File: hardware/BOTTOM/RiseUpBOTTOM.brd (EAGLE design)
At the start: 33 x 33 mm, 31 parts, among them U1 AD5242-SO16

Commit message: Updated Bottom board from Take 2
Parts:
- added J1: (no value), LinnesLab-Connectors:1X07
- moved R17 5.33 mm to (14.0, 30.5)
- moved R22 4.16 mm to (6.15, 24.3)
- moved R16 3.93 mm to (17.7, 11.4)
- moved IMU1 3.46 mm to (13.1, 7.62)
- moved C22 3.11 mm to (21.4, 7.29)
- moved U$4 3.00 mm to (21.6, 11.0)
- moved R24 2.80 mm to (14.2, 21.0)
- moved C20 2.20 mm to (14.2, 27.2)
- moved R15 2.04 mm to (31.6, 18.3)
- moved C1 1.83 mm to (6.78, 6.53)
- moved R19 1.82 mm to (6.12, 30.5)
- moved C18 1.57 mm to (14.5, 14.4)
- moved U1 1.42 mm to (29.2, 9.45)
- moved C17 1.22 mm to (14.2, 23.6)
- moved C16 1.16 mm to (27.8, 18.3)
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
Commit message: Updates end of July2nd, Start Take 03
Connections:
- removed net LED.CTRL: U$4.8
- removed net PPG: C21.2, OP3.1, U1.14
- removed net TIA: C10.2, C15.1, OP4.1, U1.3
- new net A6/TIA: C10.2, C15.1, J1.5, OP4.1, U1.3
- new net A7/PPG: C21.2, J1.7, OP3.1, U1.14
- new net D29/LED.CTRL: J1.6, U$4.8
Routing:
- added copper zone on layer 16, net GDN
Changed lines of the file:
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@@
 <setting verticaltext="up"/>
 </settings>
-<grid distance="1" unitdist="mil" unit="mm" style="lines" multiple="1" display="no" altdistance="5" altunitdist="mil" altunit="mil"/>
+<grid distance="0.1" unitdist="mil" unit="mil" style="lines" multiple="1" display="no" altdistance="5" altunitdist="mil" altunit="mil"/>
 <layers>
 <layer number="1" name="Top" color="4" fill="1" visible="yes" active="yes"/>
@@
 <wire x1="9.7028" y1="20.2332" x2="10.6528" y2="20.2332" width="0" layer="19" extent="1-1"/>
 <wire x1="13.6026" y1="14.3764" x2="10.6528" y2="20.2332" width="0" layer="19" extent="1-1"/>
-<wire x1="5.2968" y1="26.5684" x2="13.3994" y2="23.6474" width="0" layer="19" extent="1-1"/>
-<wire x1="5.2714" y1="30.48" x2="5.2968" y2="26.5684" width="0" layer="19" extent="1-1"/>
 <wire x1="10.5156" y1="8.89" x2="13.6026" y2="14.3764" width="0" layer="19" extent="1-1"/>
 <wire x1="6.7818" y1="7.3778" x2="10.5156" y2="8.89" width="0" layer="19" extent="1-1"/>
-<wire x1="21.9502" y1="9.7964" x2="13.6026" y2="14.3764" width="0" layer="19" extent="1-1"/>
+<wire x1="5.2968" y1="26.5684" x2="9.7028" y2="20.2332" width="0" layer="19" extent="1-1"/>
+<wire x1="5.2714" y1="30.48" x2="5.2968" y2="26.5684" width="0" layer="19" extent="1-1"/>
+<wire x1="22.794" y1="15.4592" x2="20.27" y2="24.08" width="0" layer="19" extent="1-1"/>
+<wire x1="21.9502" y1="9.7964" x2="22.794" y2="15.4592" width="0" layer="19" extent="1-1"/>
 <wire x1="20.5622" y1="7.2898" x2="21.9502" y2="9.7964" width="0" layer="19" extent="1-1"/>
-<wire x1="22.794" y1="15.4592" x2="21.9502" y2="9.7964" width="0" layer="19" extent="1-1"/>
-<wire x1="32.2834" y1="8.8138" x2="22.794" y2="15.4592" width="0" layer="19" extent="1-1"/>
+<wire x1="32.2834" y1="8.8138" x2="21.9502" y2="9.7964" width="0" layer="19" extent="1-1"/>
 <wire x1="32.2834" y1="7.5438" x2="32.2834" y2="8.8138" width="0" layer="19" extent="1-1"/>
 <wire x1="32.2834" y1="6.2738" x2="32.2834" y2="7.5438" width="0" layer="19" extent="1-1"/>
@@
 <contactref element="C1" pad="2"/>
 <polygon width="0.1524" layer="1" isolate="0.1778">
-<vertex x="3.4544" y="34.7218"/>
-<vertex x="34.417" y="34.7218"/>
-<vertex x="34.417" y="3.175"/>
-<vertex x="3.4798" y="3.175"/>
-<vertex x="3.4798" y="34.6964"/>
+<vertex x="3.16991875" y="34.711640625"/>
+<vertex x="34.889440625" y="34.711640625"/>
+<vertex x="34.889440625" y="3.16991875"/>
+<vertex x="3.16991875" y="3.16991875"/>
 </polygon>
 </signal>
@@
 <wire x1="15.5956" y1="6.35" x2="22.6002" y2="9.7964" width="0" layer="19" extent="1-1"/>
 </signal>
-<signal name="TIA">
+<signal name="A6/TIA">
 <contactref element="C10" pad="2"/>
 <contactref element="U1" pad="3"/>
 <contactref element="C15" pad="1"/>
 <contactref element="OP4" pad="1"/>
+<contactref element="J1" pad="5"/>
 <wire x1="22.7076" y1="33.5398" x2="24.638" y2="32.1428" width="0" layer="19" extent="1-1"/>
-<wire x1="8.7528" y1="20.2332" x2="22.7076" y2="33.5398" width="0" layer="19" extent="1-1"/>
+<wire x1="15.16" y1="33" x2="22.7076" y2="33.5398" width="0" layer="19" extent="1-1"/>
+<wire x1="8.7528" y1="20.2332" x2="15.16" y2="33" width="0" layer="19" extent="1-1"/>
 <wire x1="26.1366" y1="11.3538" x2="8.7528" y2="20.2332" width="0" layer="19" extent="1-1"/>
 </signal>
@@
 <wire x1="16.8792" y1="11.43" x2="20.6502" y2="9.7964" width="0" layer="19" extent="1-1"/>
 </signal>
-<signal name="LED.CTRL">
+<signal name="D29/LED.CTRL">
 <contactref element="U$4" pad="8"/>
+<contactref element="J1" pad="6"/>
+<wire x1="20.6502" y1="12.1492" x2="17.7" y2="33" width="0" layer="19" extent="1-1"/>
 </signal>
 <signal name="N$10">
@@
 <contactref element="R17" pad="1"/>
 <contactref element="R18" pad="2"/>
-<wire x1="13.3962" y1="30.48" x2="32.1148" y2="29.6926" width="0" layer="19" extent="1-1"/>
-<wire x1="14.7216" y1="28.6766" x2="13.3962" y2="30.48" width="0" layer="19" extent="1-1"/>
+<wire x1="14.7216" y1="28.6766" x2="32.1148" y2="29.6926" width="0" layer="19" extent="1-1"/>
+<wire x1="13.3962" y1="30.48" x2="14.7216" y2="28.6766" width="0" layer="19" extent="1-1"/>
 </signal>
 <signal name="LED">
@@
 <contactref element="U1" pad="1"/>
 </signal>
-<signal name="PPG">
+<signal name="A7/PPG">
 <contactref element="U1" pad="14"/>
 <contactref element="C21" pad="2"/>
 <contactref element="OP3" pad="1"/>
-<wire x1="12.9404" y1="17.7292" x2="26.9148" y2="32.2326" width="0" layer="19" extent="1-1"/>
+<contactref element="J1" pad="7"/>
+<wire x1="20.24" y1="33" x2="26.9148" y2="32.2326" width="0" layer="19" extent="1-1"/>
+<wire x1="12.9404" y1="17.7292" x2="20.24" y2="33" width="0" layer="19" extent="1-1"/>
 <wire x1="32.2834" y1="11.3538" x2="12.9404" y2="17.7292" width="0" layer="19" extent="1-1"/>
 </signal>
@@
 <wire x1="15.0994" y1="21.0312" x2="15.0232" y2="27.178" width="0" layer="19" extent="1-1"/>
 </signal>
+<signal name="GDN">
+<polygon width="0.1524" layer="16" isolate="0.1778">
+<vertex x="2.872740625" y="35.17138125"/>
+<vertex x="35.26028125" y="35.17138125"/>
+<vertex x="35.26028125" y="2.733040625"/>
+<vertex x="2.8702" y="2.733040625"/>
+<vertex x="2.8702" y="35.17138125"/>
+</polygon>
+</signal>
 </signals>

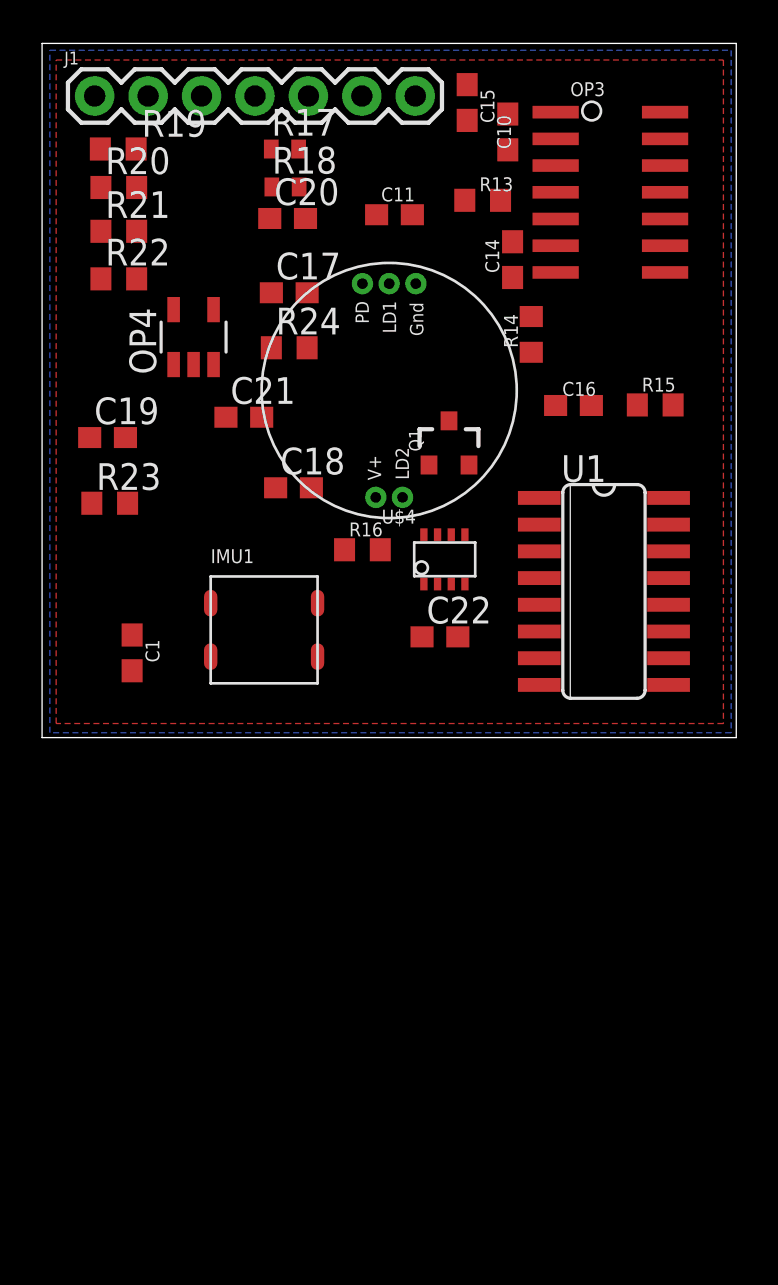
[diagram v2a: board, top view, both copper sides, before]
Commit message: placing bottom board components
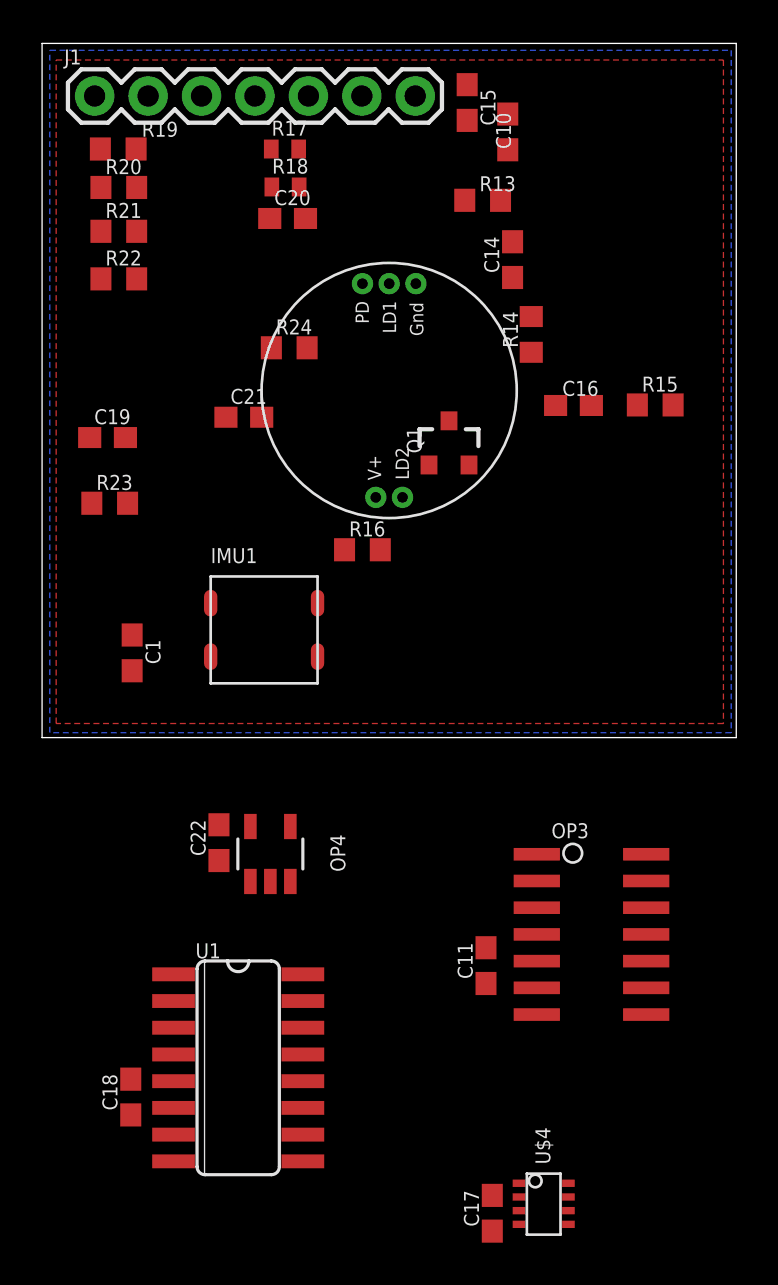
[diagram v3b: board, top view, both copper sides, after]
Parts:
- moved C17 44.8 mm to (23.9, -20.1), turned to 90 degrees
- moved C11 36.0 mm to (23.6, -8.34), turned to 90 degrees
- moved OP3 35.3 mm to (28.6, -6.86)
- moved U$4 31.0 mm to (26.3, -19.7), turned to 270 degrees
- moved C18 30.0 mm to (6.72, -14.6), turned to 90 degrees
- moved U1 28.6 mm to (11.8, -13.2)
- moved OP4 24.8 mm to (13.4, -3.03)
- moved C22 14.4 mm to (10.9, -2.49), turned to 90 degrees

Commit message: Updated Bottom board Take 3
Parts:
- moved C17 45.9 mm to (7.54, 22.7)
- moved U$4 41.4 mm to (10.4, 18.5)
- moved R19 33.5 mm to (32.4, 9.63), turned to 270 degrees
- moved R20 32.6 mm to (29.3, 5.71), turned to 180 degrees
- moved C15 29.3 mm to (29.3, 4.14), turned to 0 degrees
- moved R21 27.3 mm to (32.0, 17.9), turned to 270 degrees
- moved R23 25.3 mm to (29.3, 22.7), turned to 180 degrees
- moved C19 24.0 mm to (29.3, 20.9), turned to 180 degrees
- moved C18 24.0 mm to (5.99, 9.41), turned to 270 degrees
- moved C22 23.8 mm to (14.2, 21.1)
- moved R22 23.7 mm to (29.3, 19.0)
- moved OP4 23.6 mm to (16.9, 20.3)
- moved R13 23.6 mm to (32.4, 6.22), turned to 270 degrees
- moved U1 23.2 mm to (11.2, 9.98)
- moved C20 21.9 mm to (21.7, 6.55), turned to 270 degrees
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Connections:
- removed net LED: Q1.3
- net 3.3V: now also J1.4
- net GND: now also J1.3
- net LED.C: now also Q1.3
- net SCL: now also J1.2
- net SDA: now also J1.1
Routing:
- net A6/TIA: track 0.00 -> 35.1 mm, vias 0 -> 2
- net PD.C: track 0.00 -> 23.6 mm, vias 0 -> 2
- net N$19: track 0.00 -> 22.9 mm
- net GND: track 0.00 -> 19.4 mm, vias 0 -> 8
- net G.W2: track 0.00 -> 15.6 mm, vias 0 -> 2
- net A7/PPG: track 0.00 -> 15.5 mm
- net N$17: track 0.00 -> 9.54 mm, vias 0 -> 2
- net N$13: track 0.00 -> 6.54 mm
- net N$18: track 0.00 -> 6.16 mm
- net N$15: track 0.00 -> 5.80 mm
- net N$16: track 0.00 -> 4.17 mm
- net N$10: track 0.00 -> 3.75 mm
- net SDA: track 0.00 -> 2.22 mm
- net SCL: track 0.00 -> 2.22 mm
- net N$20: track 0.00 -> 1.74 mm
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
